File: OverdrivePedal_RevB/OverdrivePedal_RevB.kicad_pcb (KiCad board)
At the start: 2 copper layers, 26.7 x 34.9 mm, 30 parts, among them J1 AudioJack2, J2 Barrel_Jack, J3 Conn_01x03, J5 Conn_01x03, J6 AudioJack2, U2 TL071, U3 TPS60400, U4 KIA78L05T

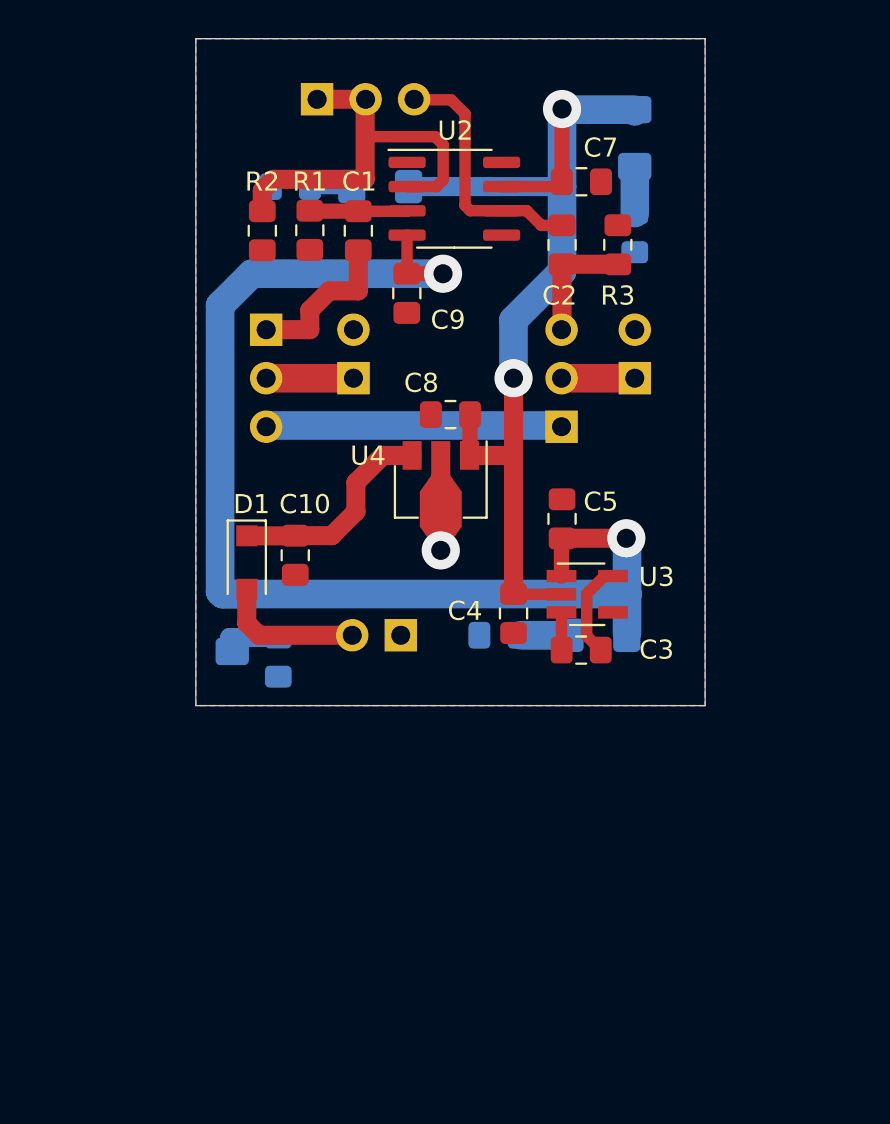
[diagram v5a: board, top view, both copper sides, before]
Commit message: Draft layout completed
RevB layout
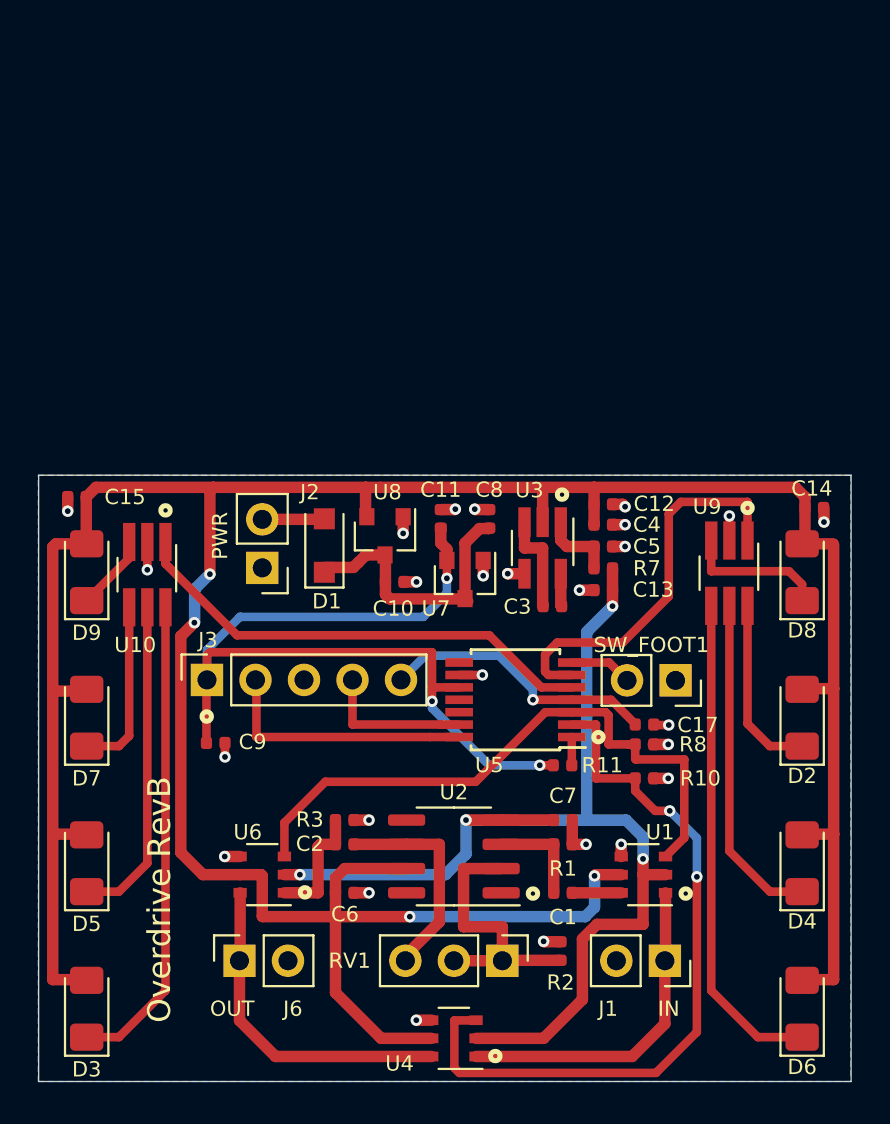
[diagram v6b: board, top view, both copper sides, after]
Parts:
- removed J5: Conn_01x03, Connector_PinHeader_2.54mm:PinHeader_1x03_P2.54mm_Vertical
- removed R4, R5, R6, R9: 1K, Resistor_SMD:R_0805_2012Metric_Pad1.15x1.40mm_HandSolder
- added C11: 10uF, Capacitor_SMD:C_0402_1005Metric, F.Cu at (71.9, 192.8)
- added C12: 10uF, Capacitor_SMD:C_0402_1005Metric, F.Cu at (80.4, 192.0)
- added C13: 1nF, Capacitor_SMD:C_0402_1005Metric, F.Cu at (80.4, 196.5)
- added C14: 1u, Capacitor_SMD:C_0402_1005Metric, F.Cu at (91.4, 192.2)
- added C15: 1u, Capacitor_SMD:C_0402_1005Metric, F.Cu at (52.8, 191.6)
- added C17: 100nF, Capacitor_SMD:C_0402_1005Metric, F.Cu at (82.5, 203.6)
- added C6: 100nF, Capacitor_SMD:C_0402_1005Metric, F.Cu at (66.9, 212.4)
- added D6: LED, LED_SMD:LED_1206_3216Metric_Pad1.42x1.75mm_HandSolder, F.Cu at (90.8, 218.4)
- added D7: LED, LED_SMD:LED_1206_3216Metric_Pad1.42x1.75mm_HandSolder, F.Cu at (53.3, 203.2)
- added D8: LED, LED_SMD:LED_1206_3216Metric_Pad1.42x1.75mm_HandSolder, F.Cu at (90.8, 195.6)
- added D9: LED, LED_SMD:LED_1206_3216Metric_Pad1.42x1.75mm_HandSolder, F.Cu at (53.3, 195.6)
- added R10: 10K, Resistor_SMD:R_0402_1005Metric, F.Cu at (82.5, 206.4)
- added R11: 10K, Resistor_SMD:R_0402_1005Metric, F.Cu at (78.3, 205.7)
- added R7: 100R, Resistor_SMD:R_0402_1005Metric, F.Cu at (80.4, 195.4)
- added R8: 10K, Resistor_SMD:R_0402_1005Metric, F.Cu at (82.5, 204.6)
- added SW_FOOT1: SW_SPST, Connector_PinSocket_2.54mm:PinSocket_1x02_P2.54mm_Vertical, F.Cu at (84.2, 201.2)
- added U1: DG468DV_T1_E3, Package_SO:TSOP-6_1.65x3.05mm_P0.95mm, F.Cu at (82.5, 211.4)
- added U10: PAM2812, Package_TO_SOT_SMD:TSOT-23-6_HandSoldering, F.Cu at (56.5, 195.7)
- added U5: STM32L011D4Px, Package_SO:TSSOP-14_4.4x5mm_P0.65mm, F.Cu at (75.8, 202.3)
- added U6: DG468DV_T1_E3, Package_SO:TSOP-6_1.65x3.05mm_P0.95mm, F.Cu at (62.5, 211.4)
- added U7: SE8233X2, Package_TO_SOT_SMD:SOT-23, F.Cu at (73.2, 196.0)
- added U8: SE8250X2, Package_TO_SOT_SMD:SOT-23, F.Cu at (69.0, 193.7)
- added U9: PAM2812, Package_TO_SOT_SMD:TSOT-23-6_HandSoldering, F.Cu at (87.0, 195.6)
- C1, C3, C4, C5, C7, C9: footprint Capacitor_SMD:C_0805_2012Metric_Pad1.15x1.40mm_HandSolder -> Capacitor_SMD:C_0402_1005Metric
- C10: value 330nF -> 1uF; footprint Capacitor_SMD:C_0805_2012Metric_Pad1.15x1.40mm_HandSolder -> Capacitor_SMD:C_0402_1005Metric
- C2: value 1uF -> C; footprint Capacitor_SMD:C_0805_2012Metric_Pad1.15x1.40mm_HandSolder -> Capacitor_SMD:C_0402_1005Metric
- C8: value 100nF -> 1uF; footprint Capacitor_SMD:C_0805_2012Metric_Pad1.15x1.40mm_HandSolder -> Capacitor_SMD:C_0402_1005Metric
- D2, D3, D4, D5, J2, RV1: moved to F.Cu
- J1, J6: value AudioJack2 -> AudioJack2-Connector; footprint Connector_PinHeader_2.54mm:PinHeader_1x02_P2.54mm_Vertical -> Connector_PinSocket_2.54mm:PinSocket_1x02_P2.54mm_Vertical; moved to F.Cu
- J3: value Conn_01x03 -> Conn_01x05; footprint Connector_PinHeader_2.54mm:PinHeader_1x03_P2.54mm_Vertical -> Connector_PinSocket_2.54mm:PinSocket_1x05_P2.54mm_Vertical; moved to F.Cu
- R1, R2, R3: footprint Resistor_SMD:R_0805_2012Metric_Pad1.15x1.40mm_HandSolder -> Resistor_SMD:R_0402_1005Metric
- U4: value KIA78L05T -> DG468DV_T1_E3; footprint Package_TO_SOT_SMD:SOT-89-3 -> Package_SO:TSOP-6_1.65x3.05mm_P0.95mm
- moved D3 53.9 mm to (53.3, 218.4)
- moved RV1 46.1 mm to (75.1, 215.9)
- moved R2 40.8 mm to (78.2, 215.4), turned to 90 degrees
- moved D5 38.6 mm to (53.3, 210.8), turned to 90 degrees
- moved J6 36.9 mm to (61.3, 215.9), turned to 90 degrees
- moved C1 36.3 mm to (78.3, 212.4), turned to 0 degrees
- moved R1 34.8 mm to (78.3, 209.8), turned to 0 degrees
- moved J1 34.6 mm to (83.6, 215.9), turned to 270 degrees
- moved U2 34.4 mm to (72.6, 210.5), turned to 180 degrees
- moved C7 33.4 mm to (78.3, 208.6)
- moved C2 33.4 mm to (66.9, 209.8), turned to 0 degrees
- moved R3 33.3 mm to (66.9, 208.6), turned to 0 degrees
- moved D4 32.4 mm to (90.8, 210.8), turned to 90 degrees
- moved U4 29.1 mm to (72.6, 220.0), turned to 180 degrees
- moved C9 25.6 mm to (60.1, 204.5), turned to 0 degrees
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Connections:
- C5 pad 1: -5V -> Net-(C5-Pad1)
- C7 pad 1: +5V -> -5V
- C8 pad 1: +5V -> /PosNeg5V_PSU/+9V_POL
- C9 pad 1: -5V -> +3V3
- D2 pad 1: -5V -> Net-(D2-Pad1)
- D2 pad 2: Net-(D2-Pad2) -> +5V
- D4 pad 1: -5V -> Net-(D4-Pad1)
- D4 pad 2: Net-(D4-Pad2) -> +5V
- J3 pad 1: Net-(C1-Pad2) -> +3V3
- J3 pad 2: Net-(J1-Pad1) -> /SYS_SWCLK
- J3 pad 3: Net-(J3-Pad3) -> GNDS
- J6 pad 1: Net-(J5-Pad2) -> Net-(J6-Pad1)
- U3 pad 1: -5V -> Net-(C5-Pad1)
- U4 pad 1: +5V -> Net-(J1-Pad1)
- U4 pad 2: GNDS -> -5V
- U4 pad 3: /PosNeg5V_PSU/+9V_POL -> /CLEAN_ENABLE
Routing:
- net +5V: track 52.9 -> 171.0 mm, vias 2 -> 4
- net +3V3: track 0.00 -> 47.3 mm, vias 0 -> 3
- net /CLEAN_ENABLE: track 0.00 -> 38.5 mm, vias 0 -> 2
- net /FX_ENABLE: track 0.00 -> 33.0 mm
- net Net-(D6-Pad1): track 0.00 -> 25.9 mm
- net /TIM2_CH1_PWM: track 0.00 -> 25.1 mm
- net Net-(D3-Pad1): track 2.31 -> 25.2 mm
- net GNDS: track 0.00 -> 22.8 mm, vias 1 -> 26
- net /TIM2_CH2_PWM: track 0.00 -> 20.8 mm
- net Net-(J6-Pad1): track 0.00 -> 17.5 mm
- net Net-(D4-Pad1): track 0.00 -> 17.5 mm
- net Net-(J3-Pad3): track 15.5 -> 0.00 mm
- net Net-(D5-Pad1): track 2.19 -> 17.2 mm
- net /SYS_NRST: track 0.00 -> 14.6 mm, vias 0 -> 1
- net /SYS_SWCLK: track 0.00 -> 13.6 mm
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- removed copper zone on F.Cu, net GNDS
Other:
- board size 26.7 x 34.9 mm -> 42.5 x 31.8 mm
- board text added: "IN"
- board text added: "OUT"
- board text added: "Overdrive RevB"
- board text added: "PWR"

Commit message: updated draft
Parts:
- added C16: 1uF, Capacitor_SMD:C_0402_1005Metric, F.Cu at (130.2, 109.1)
- added C18: 1uF, Capacitor_SMD:C_0402_1005Metric, F.Cu at (132.7, 104.2)
- added C19: 1uF, Capacitor_SMD:C_0402_1005Metric, F.Cu at (130.2, 107.9)
- added C20: 1nF, Capacitor_SMD:C_0402_1005Metric, F.Cu at (130.2, 105.3)
- added R5: 100R, Resistor_SMD:R_0402_1005Metric, F.Cu at (130.2, 106.6)
- added TP1: TestPoint, TestPoint:TestPoint_Pad_1.0x1.0mm, F.Cu at (156.7, 109.8)
- added TP2: TestPoint, TestPoint:TestPoint_Pad_1.0x1.0mm, F.Cu at (155.7, 88.5)
- added TP3: TestPoint, TestPoint:TestPoint_Pad_1.0x1.0mm, F.Cu at (131.9, 87.3)
- added TP4: TestPoint, TestPoint:TestPoint_Pad_1.0x1.0mm, F.Cu at (137.8, 95.2)
- added TP5: TestPoint, TestPoint:TestPoint_Pad_1.0x1.0mm, F.Cu at (132.0, 82.9)
- added TP6: TestPoint, TestPoint:TestPoint_Pad_1.0x1.0mm, F.Cu at (132.1, 95.2)
- added TP7: TestPoint, TestPoint:TestPoint_Pad_1.0x1.0mm, F.Cu at (150.7, 108.0)
- added U11: TPS60400, Package_TO_SOT_SMD:SOT-23-5_HandSoldering, F.Cu at (133.2, 107.2)
- C10, C8: footprint Capacitor_SMD:C_0402_1005Metric -> Capacitor_SMD:C_0805_2012Metric_Pad1.15x1.40mm_HandSolder
- moved J6 134.9 mm to (138.2, 105.1), turned to 0 degrees
- moved D3 133.7 mm to (125.7, 106.0)
- moved D6 133.7 mm to (163.2, 106.0)
- moved D4 133.2 mm to (163.2, 99.1)
- moved D5 133.2 mm to (125.7, 99.1)
- moved U4 132.7 mm to (145.0, 108.8)
- moved D7 132.6 mm to (125.7, 92.1)
- moved D2 132.6 mm to (163.2, 92.1)
- moved C1 132.5 mm to (150.7, 101.4)
- moved C6 132.5 mm to (139.2, 101.4)
- moved R3 132.5 mm to (139.2, 97.6)
- moved RV1 132.5 mm to (147.5, 105.0)
- moved U2 132.5 mm to (145.0, 99.5)
- moved C2 132.5 mm to (139.2, 98.9)
- moved J1 132.5 mm to (156.0, 105.0)
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- renumbered SW_FOOT1 to J4
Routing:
- net +5V: track 171.0 -> 188.2 mm, vias 4 -> 2
- net -5V: track 58.6 -> 74.0 mm
- net GNDS: track 22.8 -> 34.0 mm, vias 26 -> 24
- net +3V3: track 47.3 -> 38.0 mm, vias 3 -> 4
- net Net-(C18-Pad1): track 0.00 -> 5.31 mm
- net Net-(C19-Pad1): track 0.00 -> 4.09 mm
- net /PosNeg5V_PSU/+9V_POL: track 14.5 -> 18.4 mm
- net Net-(D6-Pad1): track 25.9 -> 22.1 mm
- net Net-(D3-Pad1): track 25.2 -> 21.7 mm
- net Net-(D4-Pad1): track 17.5 -> 14.7 mm
- net Net-(D5-Pad1): track 17.2 -> 14.5 mm
- net Net-(D2-Pad1): track 9.52 -> 7.26 mm
- net Net-(D7-Pad1): track 9.18 -> 6.92 mm
- net Net-(J6-Pad1): track 17.5 -> 19.6 mm
- net /FX_ENABLE: track 33.0 -> 34.7 mm
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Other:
- board size 42.5 x 31.8 mm -> 42.5 x 30.5 mm
- board text added: "FSW"
- board text added: "Overdrive Pedal RevB"
- board text removed: "GAIN POT"
- board text removed: "Overdrive RevB"
